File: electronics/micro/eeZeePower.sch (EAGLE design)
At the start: 10 parts

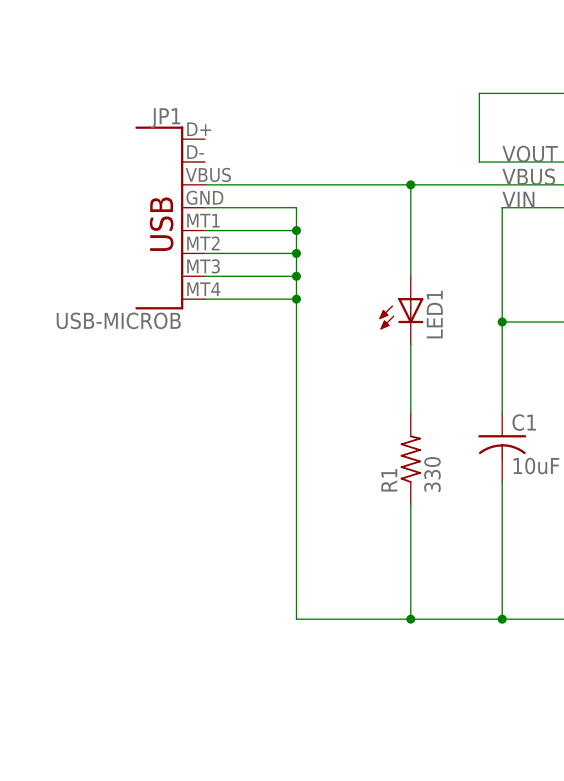
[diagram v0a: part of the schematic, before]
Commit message: microb: replaced usb micro b connector symbol & footprint
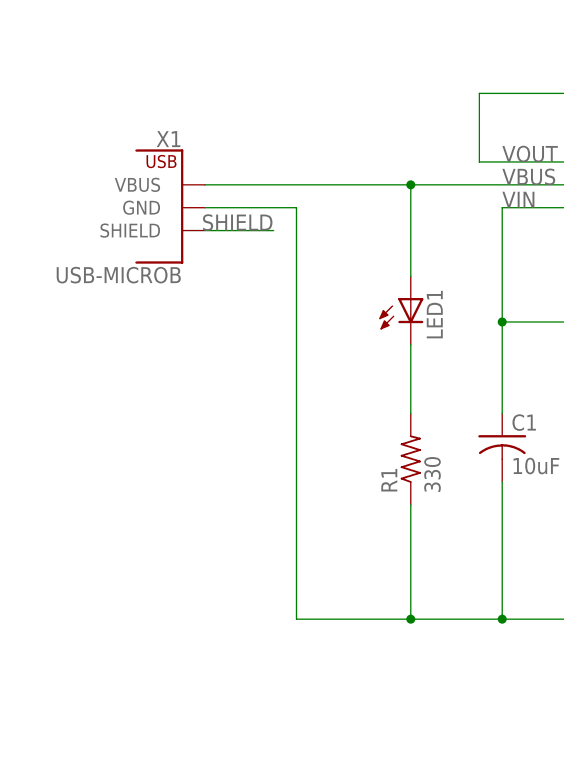
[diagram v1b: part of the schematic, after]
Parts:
- removed JP1: USB-MICROB, bt_electromech:USB-MICROB
- added X1: USB-MICROB, bt_electromech:USB_POWER-UB-4
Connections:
- new net SHIELD: X1.SHIELD
- net GND: now also X1.GND; no longer JP1.GND, JP1.SHIELD1, JP1.SHIELD2, JP1.SHIELD3, JP1.SHIELD4
- net VBUS: now also X1.VBUS; no longer JP1.VBUS
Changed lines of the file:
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@@
 <part name="JP3" library="pinhead-2" deviceset="PINHD-1X02" device="_2.54-S"/>
 <part name="JP4" library="pinhead-2" deviceset="PINHD-1X02" device="_2.54-S"/>
-<part name="JP1" library="bt_electromech" deviceset="USB" device="-MICROB"/>
+<part name="X1" library="bt_electromech" deviceset="USB_POWER" device="-UB-4" value="USB-MICROB"/>
 </parts>
 <sheets>
@@
 <instance part="JP3" gate="A" x="182.88" y="114.3"/>
 <instance part="JP4" gate="A" x="182.88" y="129.54"/>
-<instance part="JP1" gate="G$1" x="48.26" y="116.84" rot="MR0"/>
+<instance part="X1" gate="X1" x="48.26" y="114.3" rot="MR0"/>
 </instances>
 <busses>
@@
 <wire x1="83.82" y1="71.12" x2="83.82" y2="86.36" width="0.1524" layer="91"/>
 <junction x="93.98" y="71.12"/>
-<wire x1="60.96" y1="71.12" x2="60.96" y2="106.68" width="0.1524" layer="91"/>
-<wire x1="60.96" y1="106.68" x2="60.96" y2="109.22" width="0.1524" layer="91"/>
-<wire x1="60.96" y1="109.22" x2="60.96" y2="111.76" width="0.1524" layer="91"/>
-<wire x1="60.96" y1="111.76" x2="60.96" y2="114.3" width="0.1524" layer="91"/>
-<wire x1="60.96" y1="114.3" x2="60.96" y2="116.84" width="0.1524" layer="91"/>
+<wire x1="60.96" y1="71.12" x2="60.96" y2="116.84" width="0.1524" layer="91"/>
 <wire x1="83.82" y1="71.12" x2="73.66" y2="71.12" width="0.1524" layer="91"/>
 <pinref part="R1" gate="G$1" pin="1"/>
@@
 <pinref part="JP4" gate="A" pin="2"/>
 <wire x1="121.92" y1="71.12" x2="160.02" y2="71.12" width="0.1524" layer="91"/>
-<pinref part="JP1" gate="G$1" pin="GND"/>
 <wire x1="50.8" y1="116.84" x2="60.96" y2="116.84" width="0.1524" layer="91"/>
-<pinref part="JP1" gate="G$1" pin="SHIELD2"/>
-<wire x1="50.8" y1="111.76" x2="60.96" y2="111.76" width="0.1524" layer="91"/>
-<junction x="60.96" y="111.76"/>
-<pinref part="JP1" gate="G$1" pin="SHIELD3"/>
-<wire x1="50.8" y1="109.22" x2="60.96" y2="109.22" width="0.1524" layer="91"/>
-<junction x="60.96" y="109.22"/>
-<pinref part="JP1" gate="G$1" pin="SHIELD4"/>
-<wire x1="50.8" y1="106.68" x2="60.96" y2="106.68" width="0.1524" layer="91"/>
-<junction x="60.96" y="106.68"/>
-<pinref part="JP1" gate="G$1" pin="SHIELD1"/>
-<wire x1="50.8" y1="114.3" x2="60.96" y2="114.3" width="0.1524" layer="91"/>
-<junction x="60.96" y="114.3"/>
+<pinref part="X1" gate="X1" pin="GND"/>
 </segment>
 </net>
@@
 <junction x="73.66" y="119.38"/>
 <label x="83.82" y="119.38" size="1.778" layer="95"/>
-<pinref part="JP1" gate="G$1" pin="VBUS"/>
 <wire x1="50.8" y1="119.38" x2="73.66" y2="119.38" width="0.1524" layer="91"/>
+<pinref part="X1" gate="X1" pin="VBUS"/>
 </segment>
 </net>
+<net name="SHIELD" class="0">
+<segment>
+<pinref part="X1" gate="X1" pin="SHIELD"/>
+<wire x1="50.8" y1="114.3" x2="58.42" y2="114.3" width="0.1524" layer="91"/>
+<label x="58.42" y="114.3" size="1.778" layer="95" rot="MR0"/>
+</segment>
+</net>
